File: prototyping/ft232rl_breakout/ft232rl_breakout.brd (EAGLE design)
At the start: 23.5 x 15.2 mm, 17 parts, among them J1 USB, U1 FT232RL

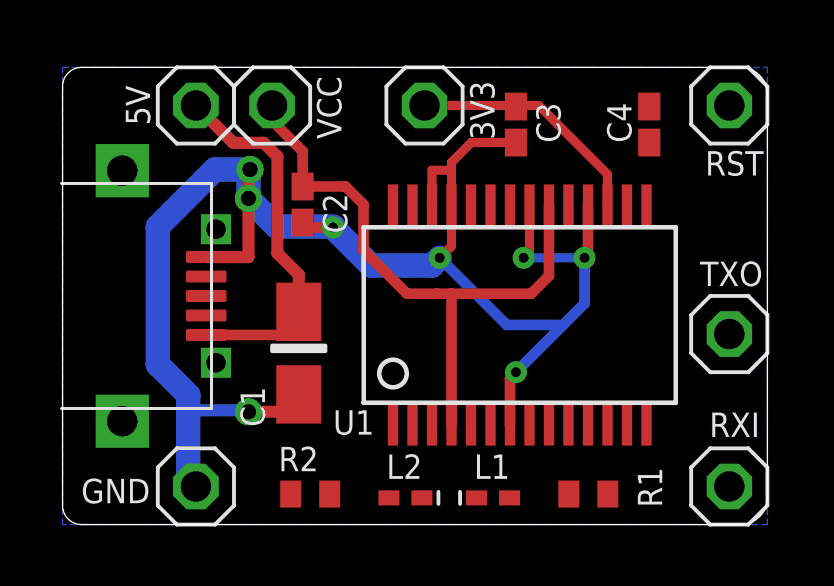
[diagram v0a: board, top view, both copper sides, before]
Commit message: Updated the placement. Ready for final auto router.
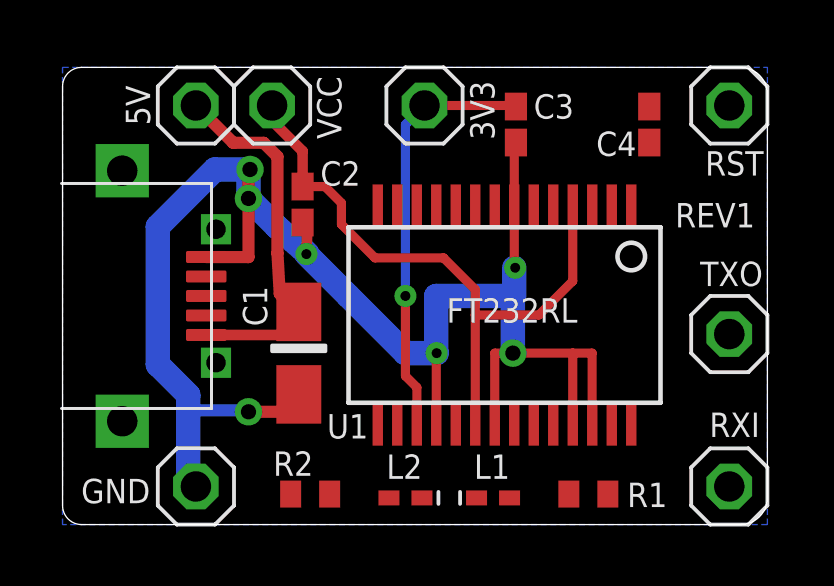
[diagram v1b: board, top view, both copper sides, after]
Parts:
- moved U1 0.51 mm to (17.9, 8.26), turned to 180 degrees
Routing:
- net N$16: track 8.09 -> 14.1 mm, vias 0 -> 1
- net N$1: track 20.7 -> 21.5 mm
- net GND: track 56.1 -> 56.7 mm, vias 8 -> 7
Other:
- board text added: "FT232RL"
- board text added: "REV1"

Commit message: Performed final auto routing.
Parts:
- D1: value LED -> RED
- D2: value LED -> GREEN
- renumbered L1 to D1, L2 to D2
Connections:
- net N$1 renamed VCC
- net N$16 renamed 3V3
- net VUSB renamed 5V
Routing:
- net VCC: track 21.5 -> 37.4 mm
- net RXI: track 0.00 -> 11.9 mm, vias 0 -> 2
- net N$10: track 0.00 -> 9.38 mm, vias 0 -> 2
- net N$15: track 0.00 -> 8.37 mm, vias 0 -> 2
- net TXO: track 0.00 -> 5.64 mm
- net N$3: track 0.00 -> 4.49 mm
- net N$2: track 0.00 -> 3.32 mm
- net RST: track 0.00 -> 2.69 mm
- net N$11: track 0.00 -> 2.61 mm
- net N$5: track 0.00 -> 2.03 mm
- net N$4: track 0.00 -> 2.03 mm

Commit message: Added tcream holes for usb connector tabs. Added bom.
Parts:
- R1, R2: value (none) -> 1K
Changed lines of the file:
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@@
 <attribute name="VALUE" x="6.35" y="12.065" size="1.27" layer="27"/>
 </element>
-<element name="R1" library="ft232rl_breakout" package="R0402" value="" x="20.701" y="2.286" smashed="yes">
+<element name="R1" library="ft232rl_breakout" package="R0402" value="1K" x="20.701" y="2.286" smashed="yes">
 <attribute name="NAME" x="21.9964" y="1.8542" size="0.8128" layer="25" font="vector" ratio="10"/>
 <attribute name="VALUE" x="20.066" y="0.381" size="1.27" layer="27"/>
 </element>
-<element name="R2" library="ft232rl_breakout" package="R0402" value="" x="11.43" y="2.286" smashed="yes" rot="R180">
+<element name="R2" library="ft232rl_breakout" package="R0402" value="1K" x="11.43" y="2.286" smashed="yes" rot="R180">
 <attribute name="NAME" x="11.5316" y="3.7084" size="0.8128" layer="25" font="vector" ratio="10" rot="R180"/>
 <attribute name="VALUE" x="12.065" y="4.191" size="1.27" layer="27" rot="R180"/>
